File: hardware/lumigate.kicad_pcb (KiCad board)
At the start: 4 copper layers, 74.6 x 51.4 mm, 61 parts, among them J1 XLR-3 out, J2 USB-C, J3 J3, J4 DISP SH9, Q1 MMBT3904, Q2 MMBT3904, SW1 BOOT, SW2 RST, U1 ESP32-S3-WROOM-1-N8, U2 W5500, U3 U3, U4 SY8089, U5 U5, Y1 25MHz

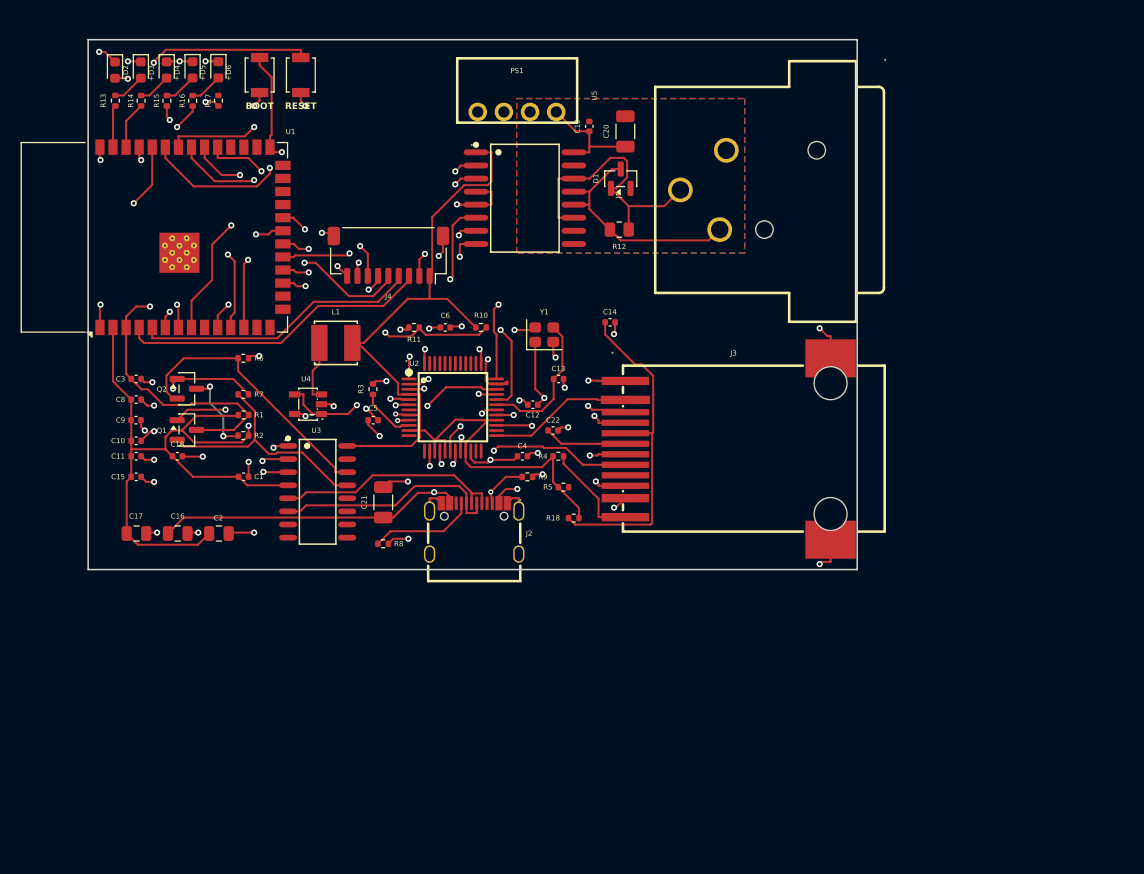
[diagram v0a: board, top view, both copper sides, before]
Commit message: hardware v4: ruggedization + grounding + plated mounting holes
Field-hardening pass for harsh / touring installs:
- USB ESD array (USBLC6) on D+/D-, self-healing PTC fuse on the USB 5V input, +5V TVS clamp
- SS54 OR diodes (lower forward drop, keeps the B0505S >=4.5V input margin once the PTC is in series)
- DMX common-mode chokes per universe (cable side, after the TVS) + ferrite filters on the isolated DC-DC rails
- wider +5V traces, fuse-coordinated and lower IR drop
- 4 plated GND mounting holes at 90x70mm spacing so the board bonds to a metal chassis at the corners
- grounding/shielding + conformal-coating notes in docs/ruggedization.md

Board routes with 0 unrouted; remaining DRC is the known JLCPCB-OK waivers (W5500 0.5mm fan-out,
USB-C CC2). Still WIP, not production ready, see hardware/VALIDATION.md.
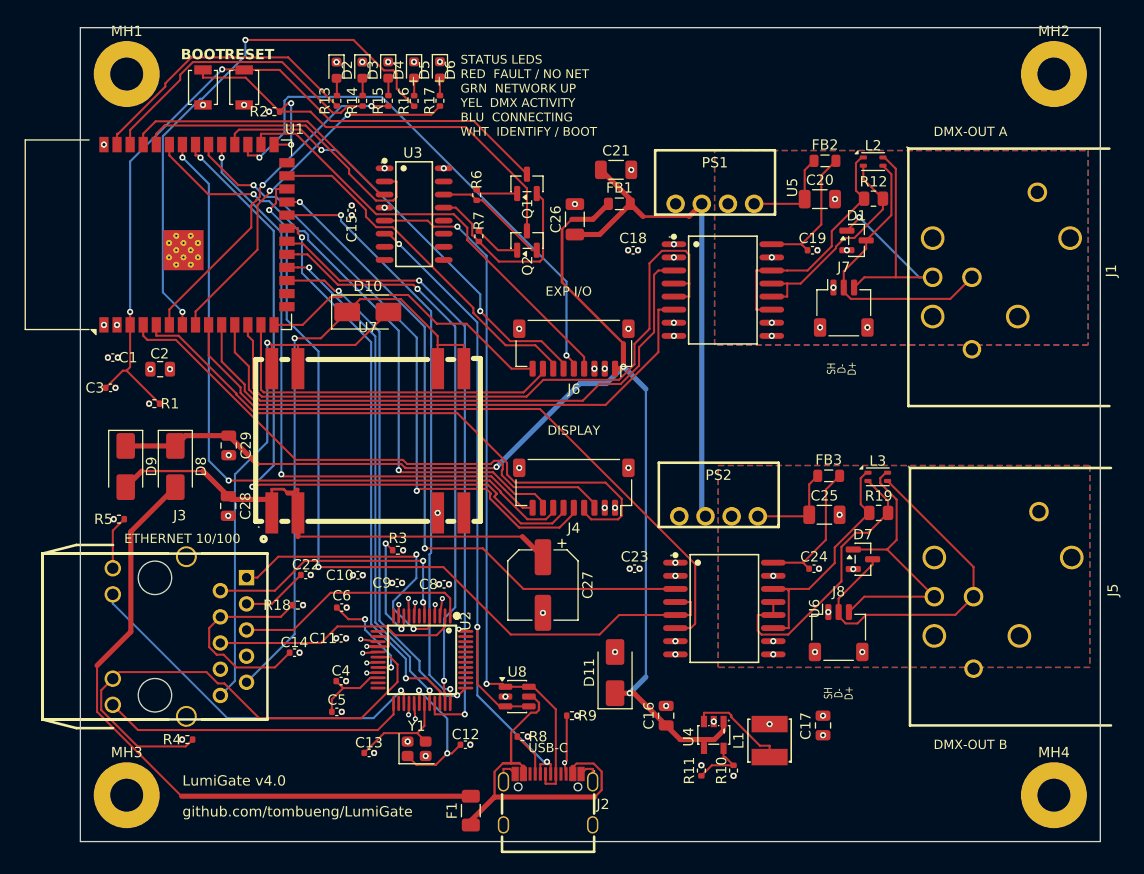
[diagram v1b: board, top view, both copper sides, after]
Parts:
- added C23: 100nF, C_0402_1005Metric, F.Cu at (151.4, 141.4)
- added C24: 100nF, C_0402_1005Metric, F.Cu at (168.8, 141.4)
- added C25: 10uF, C_1206_3216Metric, F.Cu at (169.8, 136.2)
- added C26: 10uF, C_1206_3216Metric, F.Cu at (145.6, 107.5)
- added C27: 100uF, CP_Elec_6.3x7.7, F.Cu at (142.5, 143.0)
- added C28: 10uF, C_0805_2012Metric, F.Cu at (112.0, 135.3)
- added C29: 22uF, C_0805_2012Metric, F.Cu at (112.0, 129.4)
- added D10: SMAJ58A, D_SMA, F.Cu at (125.5, 116.5)
- added D11: SMAJ5.0A, D_SMA, F.Cu at (149.5, 151.5)
- added D7: SM712, SOT-23, F.Cu at (173.6, 140.5)
- added D8: SS54, D_SMA, F.Cu at (106.8, 131.5)
- added D9: SS54, D_SMA, F.Cu at (102.0, 131.5)
- added F1: 1.5A 16V PPTC, Fuse_1206_3216Metric, F.Cu at (135.5, 164.9)
- added FB1: 600R@100MHz, L_0805_2012Metric, F.Cu at (149.9, 106.0)
- added FB2: 600R@100MHz, L_0805_2012Metric, F.Cu at (169.9, 101.8)
- added FB3: 600R@100MHz, L_0805_2012Metric, F.Cu at (170.2, 132.4)
- added J5: XLR-5 NC5FAH, CONN-TH_NC5FAH, F.Cu at (187.2, 143.5)
- added J6: EXP SH9, JST_SH_SM09B-SRSS-TB_1x09-1MP_P1.00mm_Horizontal, F.Cu at (145.5, 120.0)
- added J7: DMX-OUT A, JST_SH_SM03B-SRSS-TB_1x03-1MP_P1.00mm_Horizontal, F.Cu at (171.7, 116.1)
- added J8: DMX-OUT B, JST_SH_SM03B-SRSS-TB_1x03-1MP_P1.00mm_Horizontal, F.Cu at (171.2, 147.6)
- added L2: ACM2012-201-2P, L_CommonModeChoke_Coilank_ACM2012, F.Cu at (174.6, 101.9)
- added L3: ACM2012-201-2P, L_CommonModeChoke_Coilank_ACM2012, F.Cu at (175.0, 132.5)
- added MH1: M3 GND, MountingHole_3.2mm_M3_Pad, F.Cu at (102.1, 93.4)
- added MH2: M3 GND, MountingHole_3.2mm_M3_Pad, F.Cu at (192.1, 93.4)
- added MH3: M3 GND, MountingHole_3.2mm_M3_Pad, F.Cu at (102.1, 163.4)
- added MH4: M3 GND, MountingHole_3.2mm_M3_Pad, F.Cu at (192.1, 163.4)
- added PS2: B0505S-1W, PWRM-TH_B0505S-1W, F.Cu at (159.5, 136.3)
- added R19: 120R, R_0805_2012Metric, F.Cu at (175.1, 136.0)
- added U6: ISO3086DWR, SOIC-16_L10.3-W7.5-P1.27-LS10.3-BL, F.Cu at (160.1, 145.3)
- added U7: DP9900M-5V, PWRM-SMD_DP9900M-5V, F.Cu at (125.5, 129.0)
- added U8: USBLC6-2SC6, SOT-23-6, F.Cu at (140.0, 153.8)
- J1: value XLR-3 out -> XLR-5 NC5FAH; footprint CONN-TH_XLR-328P -> CONN-TH_NC5FAH
- J3: value J3 -> HY931147C; footprint RJ45-SMD_HR961160C -> RJ45-TH_HY931147C
- L1: value L1 -> 2.2uH
- R14, R16, R17: value 180R -> 150R
- U3: value U3 -> CH340C
- U5: value U5 -> ISO3086DWR
- moved C17 69.2 mm to (169.7, 156.6), turned to 90 degrees
- moved L1 57.1 mm to (164.5, 158.1), turned to 90 degrees
- moved J3 56.2 mm to (107.2, 148.0), turned to 0 degrees
- moved R11 51.3 mm to (157.9, 161.0), turned to 90 degrees
- moved U4 50.8 mm to (159.1, 157.6), turned to 90 degrees
- moved C16 50.6 mm to (154.5, 155.7), turned to 90 degrees
- moved R10 49.5 mm to (161.0, 161.0), turned to 90 degrees
- moved C18 48.5 mm to (151.3, 110.5)
- moved R4 45.3 mm to (108.0, 158.0)
- moved C14 44.3 mm to (118.4, 149.6)
- moved R5 43.3 mm to (101.3, 136.6)
- moved Y1 42.1 mm to (130.2, 158.9)
- moved Q1 40.7 mm to (140.9, 104.1), turned to 90 degrees
- moved C13 40.7 mm to (125.6, 159.3)
- moved C21 39.4 mm to (149.6, 102.7), turned to 0 degrees
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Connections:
- C19 pad 1: VISO -> VISO_DRV
- C21 pad 1: +5V -> +5V_DMX
- D1 pad 1: DMX_A -> DMX_AO
- D1 pad 3: DMX_B -> DMX_BO
- J1 pad 2: DMX_B -> DMX_BO
- J1 pad 3: DMX_A -> DMX_AO
- J2 pad A4B9: +5V -> +5V_USB
- J2 pad B4A9: +5V -> +5V_USB
- J3 pad 1: N$2 -> ETH_RXN
- J3 pad 10: GND -> VPOE-
- J3 pad 11: ETH_ACTLED -> N$3
- J3 pad 12: N$3 -> ETH_ACTLED
- J3 pad 13: GND -> N$2
- J3 pad 14: GND -> ETH_LINKLED
- J3 pad 2: ETH_LINKLED -> ETH_RXP
- J3 pad 3: ETH_TXP -> ETH_RCT
- J3 pad 4: ETH_TXN -> ETH_TCT
- J3 pad 5: ETH_TCT -> ETH_TXN
- J3 pad 6: ETH_RCT -> ETH_TXP
- J3 pad 7: ETH_RXP -> (no net)
- J3 pad 8: ETH_RXN -> (no net)
- J3 pad 9: (no net) -> VPOE+
- PS1 pad 2: +5V -> +5V_DMX
- Q2 pad 1: N$6 -> N$5
- R13 pad 2: N$7 -> N$6
- R14 pad 2: N$8 -> N$7
- R15 pad 2: N$9 -> N$8
- R16 pad 2: N$10 -> N$9
- R17 pad 2: N$11 -> N$10
- R4 pad 2: N$3 -> N$2
- R5 pad 2: N$4 (its old number) -> N$3
- R7 pad 2: N$6 -> N$5
- U1 pad 13: (no net) -> EXP_IO19
- U1 pad 14: (no net) -> EXP_IO20
- U1 pad 23: (no net) -> DMX2_RX
- U1 pad 24: (no net) -> DMX2_EN
- U1 pad 25: (no net) -> EXP_IO48
- U1 pad 28: (no net) -> EXP_IO35
- U1 pad 29: (no net) -> EXP_IO36
- U1 pad 30: (no net) -> EXP_IO37
- U1 pad 9: (no net) -> DMX2_TX
- U5 pad 16: VISO -> VISO_DRV
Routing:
- net +3V3: track 169.6 -> 8.91 mm, vias 2 -> 31
- net DMX2_EN: track 0.00 -> 82.4 mm, vias 0 -> 2
- net GND: track 91.3 -> 17.8 mm, vias 51 -> 62
- net DMX2_TX: track 0.00 -> 66.8 mm
- net DMX2_RX: track 0.00 -> 65.9 mm, vias 0 -> 2
- net +5V_USBF: track 0.00 -> 64.6 mm
- net VPOE+: track 0.00 -> 60.3 mm, vias 0 -> 1
- net VPOE-: track 0.00 -> 53.9 mm, vias 0 -> 1
- net EXP_IO36: track 0.00 -> 52.5 mm, vias 0 -> 2
- net +5V_POE: track 0.00 -> 50.3 mm
- net USB_DM: track 22.5 -> 72.8 mm, vias 0 -> 3
- net +5V_DMX: track 0.00 -> 49.5 mm
- net USB_DP: track 22.4 -> 69.8 mm, vias 0 -> 2
- net EXP_IO37: track 0.00 -> 44.0 mm, vias 0 -> 2
- net DISP_MOSI: track 26.7 -> 70.6 mm
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- added copper zone on In2.Cu, net +3V3
- added copper zone on B.Cu, net GNDISO2
- added copper zone on F.Cu, net GNDISO2
- removed copper zone on In2.Cu, net GND
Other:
- board size 74.6 x 51.4 mm -> 99 x 79 mm
- board text added: "BLU CONNECTING"
- board text added: "D+"
- board text added: "D-"
- board text added: "DISPLAY"
- board text added: "DMX-OUT A"
- board text added: "DMX-OUT B"
- board text added: "ETHERNET 10/100"
- board text added: "EXP I/O"
- board text added: "GRN NETWORK UP"
- board text added: "LumiGate v4.0"
- board text added: "RED FAULT / NO NET"
- board text added: "SH"
- board text added: "STATUS LEDS"
- board text added: "USB-C"
- board text added: "WHT IDENTIFY / BOOT"
- board text added: "YEL DMX ACTIVITY"
- board text added: "github.com/tombueng/LumiGate"

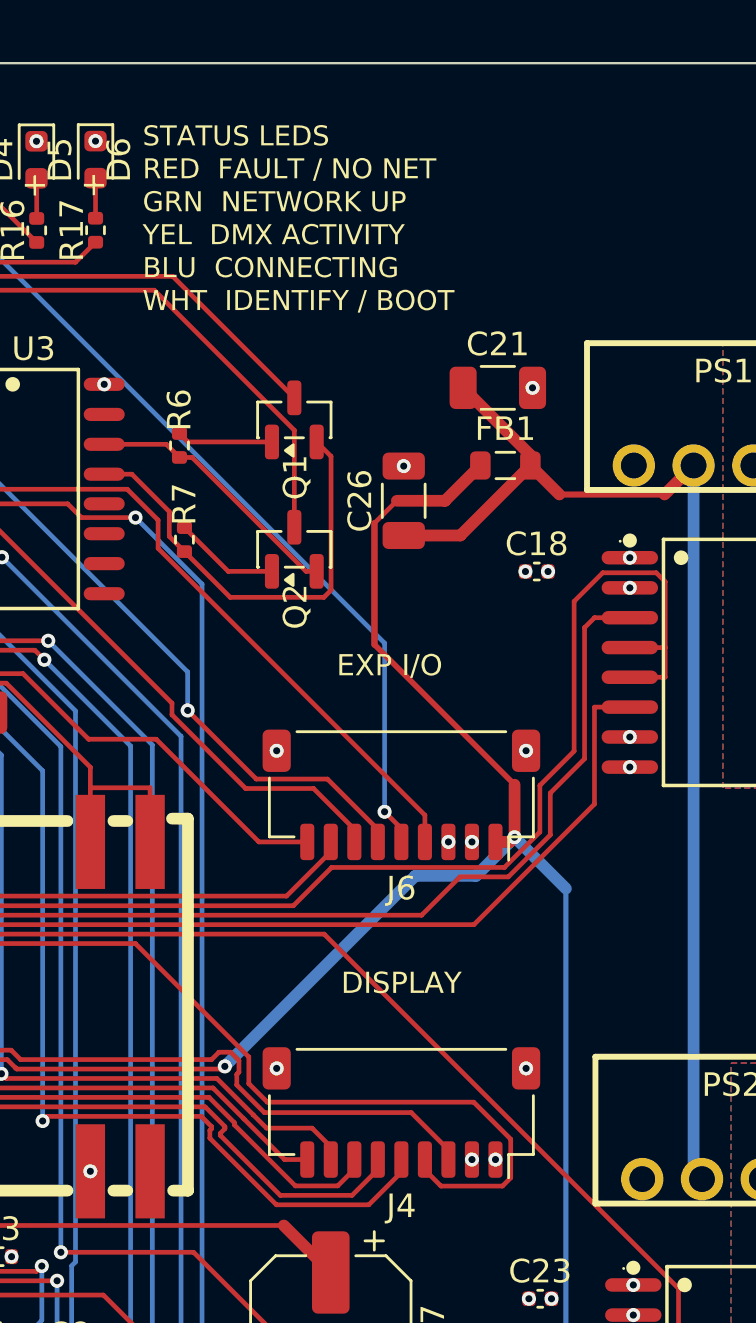
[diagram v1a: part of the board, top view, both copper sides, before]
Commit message: hardware v4: pre-fab validation pass + connector/LED pinout silk
Validation (see hardware/VALIDATION_REPORT.md + VALIDATION_PLAN.md):
- read every active part, the crystal and the connectors from official datasheets; recomputed
  ratings/values; ran the validation scripts, DRC, ERC, and SPICE (ngspice in WSL) on the power chain.
- fixed a crystal-load blocker: caps 22pF -> 33pF C0G (the part is CL=20pF, so the W5500 25MHz was
  running fast and eating the +-50ppm Ethernet budget).
- fixed EXRES1 (12k -> 12.4k 1%) and the PoE TVS (SMAJ58A -> SMAJ60A for more standoff margin).
- validated every ESP32-S3 GPIO assignment: zero must-change pins (IO35/36/37 free on the N8, strapping
  safe, no flash/input-only conflict).
- documented the one real margin: a USB-powered B0505S/ISO3086 VCC2 dips under 4.5V on a weak 5V supply
  (SPICE: needs VBUS >= ~4.95V; PoE's 5.0V gives 4.56V). Recommend a clean >=5V source or ideal-diode
  OR-ing on the next spin.

Silk: back-side gridded pinout tables for J4/J6, front Display/Expansion labels + pin-1 markers, and the
status-LED legend turned into a grid.

Board still routes 0 unrouted; DRC is the 3 known JLCPCB-OK waivers.
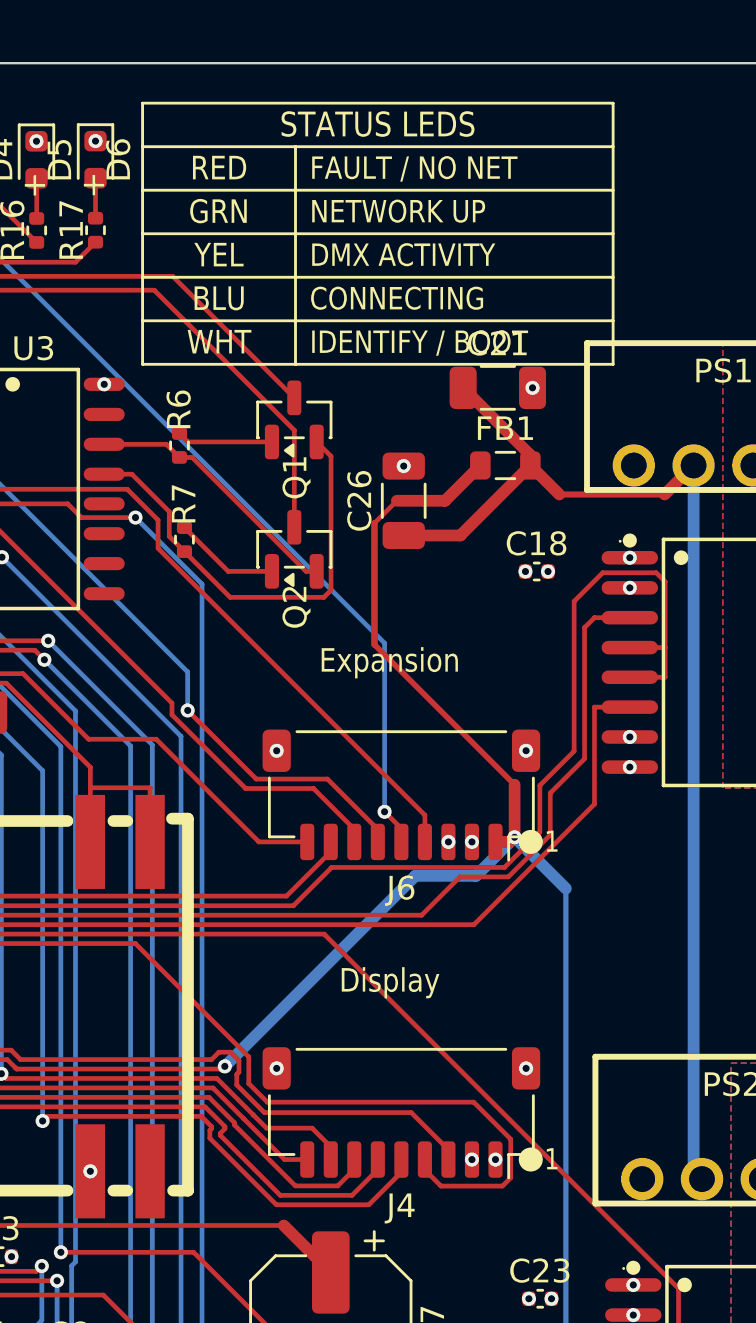
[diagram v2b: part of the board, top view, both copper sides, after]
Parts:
- C12, C13: value 22pF -> 33pF C0G
- D10: value SMAJ58A -> SMAJ60A
- R3: value 12k -> 12.4k
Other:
- board text added: "+3V3"
- board text added: "+5V"
- board text added: "-"
- board text added: "1"
- board text added: "19"
- board text added: "2"
- board text added: "20"
- board text added: "3"
- board text added: "35"
- board text added: "36"
- board text added: "37"
- board text added: "38"
- board text added: "39"
- board text added: "4"
- board text added: "40"
- board text added: "41"
- board text added: "42"
- board text added: "48"
- board text added: "5"
- board text added: "6"
- board text added: "7"
- board text added: "8"
- board text added: "9"
- board text added: "BLU"
- board text added: "CONNECTING"
- board text added: "CS"
- board text added: "DC"
- board text added: "DISPLAY J4"
- board text added: "DMX ACTIVITY"
- board text added: "Display"
- board text added: "EXPANSION J6"
- board text added: "Expansion"
- board text added: "FAULT / NO NET"
- board text added: "FUNCTION"
- board text added: "GND"
- board text added: "GPIO"
- board text added: "GRN"
- board text added: "IDENTIFY / BOOT"
- board text added: "MOSI"
- board text added: "NETWORK UP"
- board text added: "PIN"
- board text added: "RED"
- board text added: "RST"
- board text added: "SCK"
- board text added: "SCL"
- board text added: "SDA"
- board text added: "WHT"
- board text added: "YEL"
- board text removed: "BLU CONNECTING"
- board text removed: "DISPLAY"
- board text removed: "EXP I/O"
- board text removed: "GRN NETWORK UP"
- board text removed: "RED FAULT / NO NET"
- board text removed: "WHT IDENTIFY / BOOT"
- board text removed: "YEL DMX ACTIVITY"
